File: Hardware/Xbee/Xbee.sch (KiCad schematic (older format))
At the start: 36 parts, among them J1 Alimentación, J2 Raspberry, J3 Pines 1, J4 Pines 2, J5 Programación, J6 Entrada, J7 Salida, K1 SANYOU_SRD_Form_C, Q1 2N7002, Q2 AP2300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

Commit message: Battery Charger
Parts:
- added H1: PoteCarga, symbol Mechanical:MountingHole_Pad
- added H2: PoteEstado, symbol Mechanical:MountingHole_Pad
- added J8: Batería, TerminalBlock:TerminalBlock_bornier-2_P5.08mm, symbol Xbee-rescue:Screw_Terminal_01x02-Connector
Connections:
- net +12V: now also R11.2; no longer J1.2 (Pin_2)
- net GNDREF: now also J8.1 (Pin_1)
- net at RV1.2, U3.3 (+): now also H1.1
- net at RV2.2, U3.6 (-): now also H2.1
- net CargaBatería: now reaches U3.1
- net CargaBatería: no longer R11.2
- new net Bat+: J8.2 (Pin_2)
- new net Vin+: J1.2 (Pin_2)
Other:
- note added: "Comparadaor-Batería"
- note removed: "Estado-Batería"
- moved on the sheet: D1, D5, J1, J2, J6, J7, R1, R10, R11

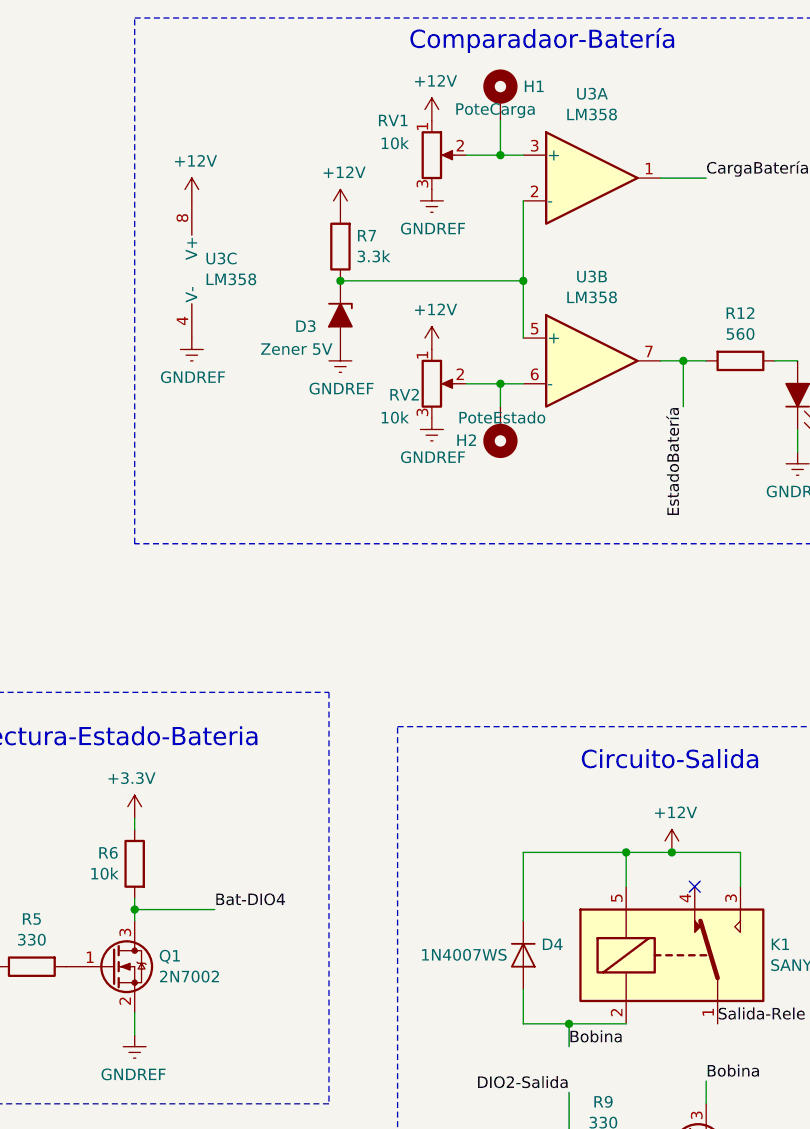
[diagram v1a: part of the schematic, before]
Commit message: Added Diodes Footprints
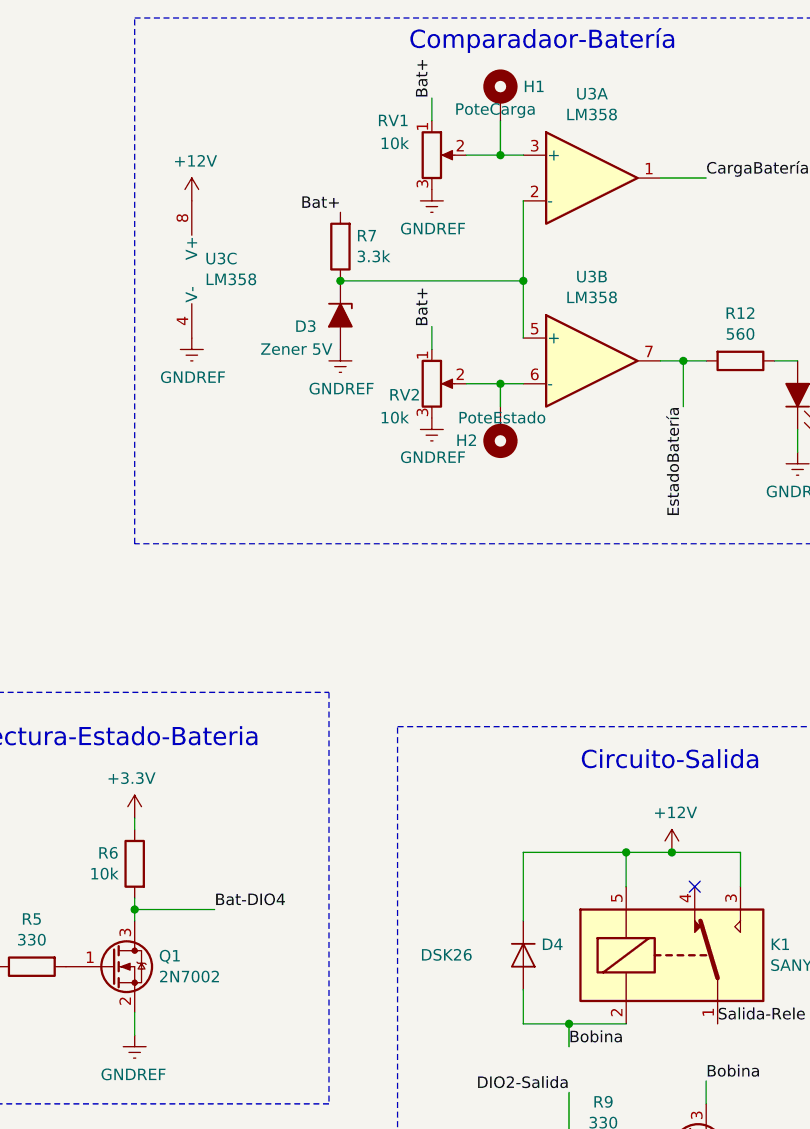
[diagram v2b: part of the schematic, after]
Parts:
- D4: value 1N4007WS -> DSK26
- H1, H2: footprint (none) -> MountingHole:MountingHole_2.2mm_M2_DIN965_Pad
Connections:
- net +12V: no longer R7.2, RV1.1, RV2.1
- net Bat+: now also R7.2, RV1.1, RV2.1
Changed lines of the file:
@@
 	-1   0    0    1
-$EndComp
-$Comp
-L Xbee-rescue:+12V-power #PWR025
-U 1 1 5C1A9FAF
-P 8350 1500
-F 0 "#PWR025" H 8350 1350 50  0001 C CNN
-F 1 "+12V" H 8365 1673 50  0000 C CNN
-F 2 "" H 8350 1500 50  0001 C CNN
-F 3 "" H 8350 1500 50  0001 C CNN
-	1    8350 1500
-	1    0    0    -1
 $EndComp
 Wire Wire Line
@@
 	9150 1800 9150 2050
 $Comp
-L Xbee-rescue:+12V-power #PWR028
-U 1 1 5C1AB703
-P 8750 1100
-F 0 "#PWR028" H 8750 950 50  0001 C CNN
-F 1 "+12V" H 8765 1273 50  0000 C CNN
-F 2 "" H 8750 1100 50  0001 C CNN
-F 3 "" H 8750 1100 50  0001 C CNN
-	1    8750 1100
-	1    0    0    -1
-$EndComp
-$Comp
 L Xbee-rescue:GNDREF-power #PWR029
 U 1 1 5C1AB747
@@
 F 3 "" H 8750 1400 50  0001 C CNN
 	1    8750 1400
-	1    0    0    -1
-$EndComp
-$Comp
-L Xbee-rescue:+12V-power #PWR030
-U 1 1 5C1AB784
-P 8750 2100
-F 0 "#PWR030" H 8750 1950 50  0001 C CNN
-F 1 "+12V" H 8765 2273 50  0000 C CNN
-F 2 "" H 8750 2100 50  0001 C CNN
-F 3 "" H 8750 2100 50  0001 C CNN
-	1    8750 2100
 	1    0    0    -1
 $EndComp
@@
 P 9150 4750
 F 0 "D4" V 9104 4829 50  0000 L CNN
-F 1 "1N4007WS" V 9150 4300 50  0000 L CNN
+F 1 "DSK26" V 9150 4300 50  0000 L CNN
 F 2 "Diode_SMD:D_SOD-323_HandSoldering" H 9150 4575 50  0001 C CNN
 F 3 "http://www.vishay.com/docs/88503/1n4001.pdf" H 9150 4750 50  0001 C CNN
@@
 F 0 "H1" H 9150 1049 50  0000 L CNN
 F 1 "PoteCarga" H 8850 950 50  0000 L CNN
-F 2 "" H 9050 1000 50  0001 C CNN
+F 2 "MountingHole:MountingHole_2.2mm_M2_DIN965_Pad" H 9050 1000 50  0001 C CNN
 F 3 "~" H 9050 1000 50  0001 C CNN
 	1    9050 1000
@@
 F 0 "H2" H 9150 2499 50  0000 L CNN
 F 1 "PoteEstado" H 8850 2400 50  0000 L CNN
-F 2 "" H 9050 2450 50  0001 C CNN
+F 2 "MountingHole:MountingHole_2.2mm_M2_DIN965_Pad" H 9050 2450 50  0001 C CNN
 F 3 "~" H 9050 2450 50  0001 C CNN
 	1    9050 2450
@@
 Wire Wire Line
 	9050 2250 9150 2250
+Text Label 8350 1500 2    50   ~ 0
+Bat+
+Text Label 8750 1000 1    50   ~ 0
+Bat+
+Wire Wire Line
+	8750 1000 8750 1100
+Text Label 8750 2000 1    50   ~ 0
+Bat+
+Wire Wire Line
+	8750 2000 8750 2100
 $EndSCHEMATC

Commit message: PCB Component placement
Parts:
- J3, J4: footprint Connector_PinSocket_2.54mm:PinSocket_1x10_P2.54mm_Vertical -> Connector_PinSocket_2.00mm:PinSocket_1x10_P2.00mm_Vertical
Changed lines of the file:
@@
 F 0 "J3" H 1200 2300 50  0000 L CNN
 F 1 "Pines 1" H 1100 2200 50  0000 L CNN
-F 2 "Connector_PinSocket_2.54mm:PinSocket_1x10_P2.54mm_Vertical" H 1350 1650 50  0001 C CNN
+F 2 "Connector_PinSocket_2.00mm:PinSocket_1x10_P2.00mm_Vertical" H 1350 1650 50  0001 C CNN
 F 3 "~" H 1350 1650 50  0001 C CNN
 	1    1350 1650
@@
 F 0 "J4" H 1470 2267 50  0000 C CNN
 F 1 "Pines 2" H 1470 2176 50  0000 C CNN
-F 2 "Connector_PinSocket_2.54mm:PinSocket_1x10_P2.54mm_Vertical" H 1550 1650 50  0001 C CNN
+F 2 "Connector_PinSocket_2.00mm:PinSocket_1x10_P2.00mm_Vertical" H 1550 1650 50  0001 C CNN
 F 3 "~" H 1550 1650 50  0001 C CNN
 	1    1550 1650

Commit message: Localización de componentes
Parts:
- SW1, SW2: symbol Xbee-rescue:SW_Push_Dual-Switch -> Xbee-rescue:SW_Push_Dual-Switch-Xbee-rescue
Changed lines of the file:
@@
 EESchema Schematic File Version 4
 LIBS:Xbee-cache
-EELAYER 30 0
+EELAYER 29 0
 EELAYER END
 $Descr A4 11693 8268
@@
 $EndComp
 $Comp
-L Xbee-rescue:SW_Push_Dual-Switch SW1
+L Xbee-rescue:SW_Push_Dual-Switch-Xbee-rescue SW1
 U 1 1 5C05513C
 P 1150 6700
@@
 $EndComp
 $Comp
-L Xbee-rescue:SW_Push_Dual-Switch SW2
+L Xbee-rescue:SW_Push_Dual-Switch-Xbee-rescue SW2
 U 1 1 5C0551E7
 P 2200 6700

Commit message: Localización 2
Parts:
- D4: footprint Diode_SMD:D_SOD-323_HandSoldering -> Diode_SMD:D_SOD-123F
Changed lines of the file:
@@
 EESchema Schematic File Version 4
 LIBS:Xbee-cache
-EELAYER 29 0
+EELAYER 30 0
 EELAYER END
 $Descr A4 11693 8268
@@
 F 0 "D4" V 9104 4829 50  0000 L CNN
 F 1 "DSK26" V 9150 4300 50  0000 L CNN
-F 2 "Diode_SMD:D_SOD-323_HandSoldering" H 9150 4575 50  0001 C CNN
+F 2 "Diode_SMD:D_SOD-123F" H 9150 4575 50  0001 C CNN
 F 3 "http://www.vishay.com/docs/88503/1n4001.pdf" H 9150 4750 50  0001 C CNN
 	1    9150 4750

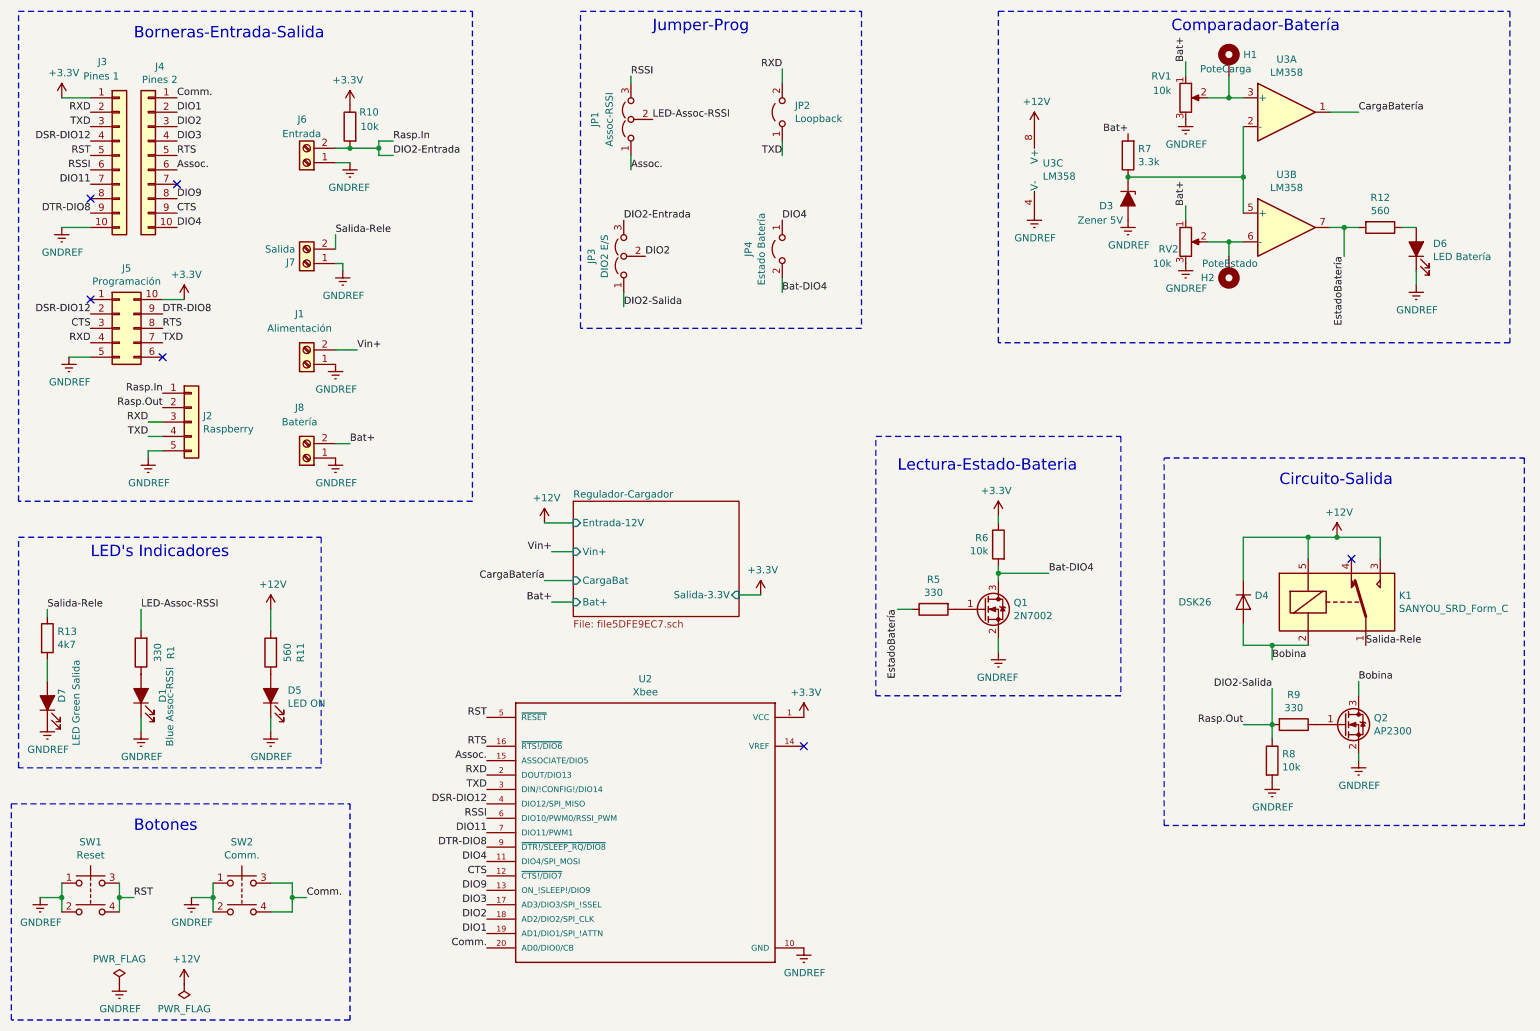
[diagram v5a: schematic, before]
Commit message: Change footprints
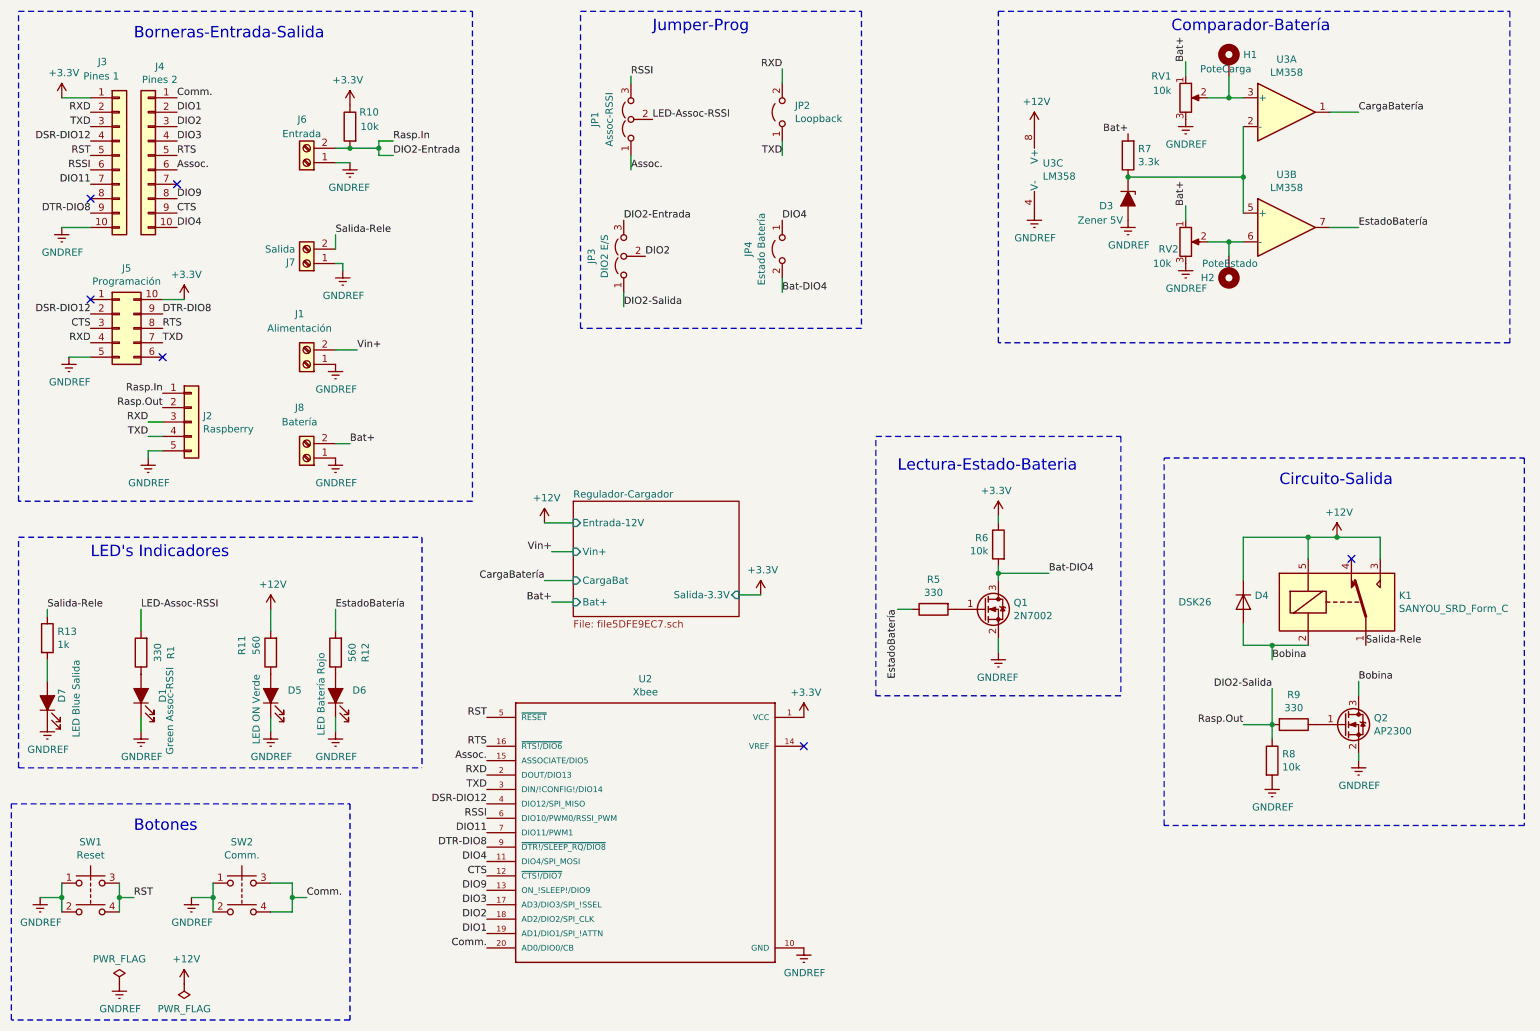
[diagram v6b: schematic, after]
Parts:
- D1: value Blue Assoc-RSSI -> Green Assoc-RSSI; footprint LED_SMD:LED_0805_2012Metric -> LED_SMD:LED_1206_3216Metric_Pad1.42x1.75mm_HandSolder; Código Proveedor 1 (none) -> 160-1169-1-ND; Link Proveedor 1 (none) -> https://www.digikey.com/product-detail/en/lite-on-inc/LTST-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; Nombre Fabricante (none) -> LTST-C150GKT; Package (none) -> 1206
- D5: value LED ON -> LED ON Verde; Código Proveedor 1 (none) -> 754-1263-ND; Link Proveedor 1 (none) -> https://www.digikey.com/product-detail/en/kingbright/WP7113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; Nombre Fabricante (none) -> WP7113GD; Package (none) -> 5mm T/H
- D6: value LED Batería -> LED Batería Rojo; Código Proveedor 1 (none) -> 754-1264-ND; Link Proveedor 1 (none) -> https://www.digikey.com/product-detail/en/kingbright/WP7113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; Nombre Fabricante (none) -> WP7113ID; Package (none) -> 5mm T/H
- D7: value LED Green Salida -> LED Blue Salida; footprint LED_SMD:LED_0805_2012Metric -> LED_SMD:LED_1206_3216Metric_Pad1.42x1.75mm_HandSolder; Código Proveedor 1 (none) -> 160-1643-1-ND; Link Proveedor 1 (none) -> https://www.digikey.com/product-detail/en/lite-on-inc/LTST-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; Nombre Fabricante (none) -> LTST-C150TBKT; Package (none) -> 1206
- JP1, JP3: Código Proveedor 1 (none) -> 732-5316-ND; Link Proveedor 1 (none) -> https://www.digikey.com/product-detail/en/w-rth-elektronik/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; Nombre Fabricante (none) -> 61300311121; Package (none) -> 2.54mm T/H
- JP2, JP4: Código Proveedor 1 (none) -> 952-2262-ND; Link Proveedor 1 (none) -> https://www.digikey.com/product-detail/en/harwin-inc/M20-99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; Nombre Fabricante (none) -> M20-9990246; Package (none) -> 2.54mm T/H
- R1: footprint Resistor_SMD:R_0805_2012Metric_Pad1.15x1.40mm_HandSolder -> Resistor_SMD:R_1206_3216Metric_Pad1.42x1.75mm_HandSolder; Código Proveedor 1 (none) -> P.33PCT-ND; Link Proveedor 1 (none) -> https://www.digikey.com/product-detail/en/panasonic-electro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; Nombre Fabricante (none) -> ERJ-8RQJR33V; Package (none) -> 1206
- R11: footprint Resistor_SMD:R_0805_2012Metric_Pad1.15x1.40mm_HandSolder -> Resistor_SMD:R_1206_3216Metric_Pad1.42x1.75mm_HandSolder; Código Proveedor 1 (none) -> P.56PCT-ND; Link Proveedor 1 (none) -> https://www.digikey.com/product-detail/en/panasonic-electro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; Nombre Fabricante (none) -> ERJ-8RQJR56V; Package (none) -> 1206
- R12: footprint Resistor_SMD:R_0805_2012Metric_Pad1.15x1.40mm_HandSolder -> Resistor_SMD:R_1206_3216Metric_Pad1.42x1.75mm_HandSolder; Código Proveedor 1 (none) -> P.56PCT-ND; Link Proveedor 1 (none) -> https://www.digikey.com/product-detail/en/panasonic-electro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; Nombre Fabricante (none) -> ERJ-8RQJR56V
- R13: value 4k7 -> 1k; footprint Resistor_SMD:R_0805_2012Metric_Pad1.15x1.40mm_HandSolder -> Resistor_SMD:R_1206_3216Metric_Pad1.42x1.75mm_HandSolder; Código Proveedor 1 (none) -> 311-1.0KERCT-ND; Link Proveedor 1 (none) -> https://www.digikey.com/product-detail/en/yageo/RC1206JR-07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; Nombre Fabricante (none) -> RC1206JR-071KL; Package (none) -> 1206
- R6: footprint Resistor_SMD:R_0805_2012Metric_Pad1.15x1.40mm_HandSolder -> Resistor_SMD:R_1206_3216Metric_Pad1.42x1.75mm_HandSolder; Código Proveedor 1 (none) -> 311-10KERCT-ND; Link Proveedor 1 (none) -> https://www.digikey.com/product-detail/en/yageo/RC1206JR-07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; Nombre Fabricante (none) -> RC1206JR-0710KL; Package (none) -> 1206
- R7: footprint Resistor_SMD:R_0805_2012Metric_Pad1.15x1.40mm_HandSolder -> Resistor_SMD:R_1206_3216Metric_Pad1.42x1.75mm_HandSolder; Código Proveedor 1 (none) -> RMCF1206JT3K30CT-ND; Link Proveedor 1 (none) -> https://www.digikey.com/product-detail/en/stackpole-electro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; Nombre Fabricante (none) -> RMCF1206JT3K30; Package (none) -> 1206
- RV1, RV2: footprint Potentiometer_THT:Potentiometer_Bourns_3386C_Horizontal -> Potentiometer_THT:Potentiometer_Vishay_T73YP_Vertical; Código Proveedor 1 (none) -> CT6EP103-ND; Link Proveedor 1 (none) -> https://www.digikey.com/product-detail/en/nidec-copal-elect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; Nombre Fabricante (none) -> CT6EP103; Package (none) -> CT-6
- U3: Código Proveedor 1 (none) -> 497-1591-1-ND; Link Proveedor 1 (none) -> https://www.digikey.com/product-detail/en/stmicroelectronic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; Nombre Fabricante (none) -> LM358DT; Package (none) -> SO-8
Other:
- note added: "Comparador-Batería"
- note removed: "Comparadaor-Batería"
- moved on the sheet: D6, R12
